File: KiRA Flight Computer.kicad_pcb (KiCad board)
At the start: 4 copper layers, 50 x 74.8 mm, 112 parts, among them IC1 SC4216HSETRT, J1 Conn_01x04_Pin, J10 Conn_01x02_Pin, J11 Conn_01x03_Pin, J12 Conn_01x03_Pin, J13 Screw_Terminal_01x02, J14 Screw_Terminal_01x02, J15 Conn_Coaxial, J2 USB_C_Receptacle_USB2.0_14P, J3 Conn_01x03_Pin, J4 Conn_01x03, J5 Conn_01x02, J6 Micro_SD_Card_Det1, J8 Conn_01x02_Pin, J9 Conn_01x03_Pin, Q1 FDMA430NZ, Q2 FDMA430NZ, SW1 SW_Push, SW2 SW_SPDT, U1 ICM-426788P, U10 BNO055, U2 STM32F407VGTx, U3 MMC5883MA, U4 DPS368, U5 NEO-M9N, U6 Wio-SX1262, U7 USBLC6-2P6, U8 TPS62933P, U9 Tudi AT24CM02-SSHD-T-TUDI, Y1 16MHz 7pF, Y2 OV_7604

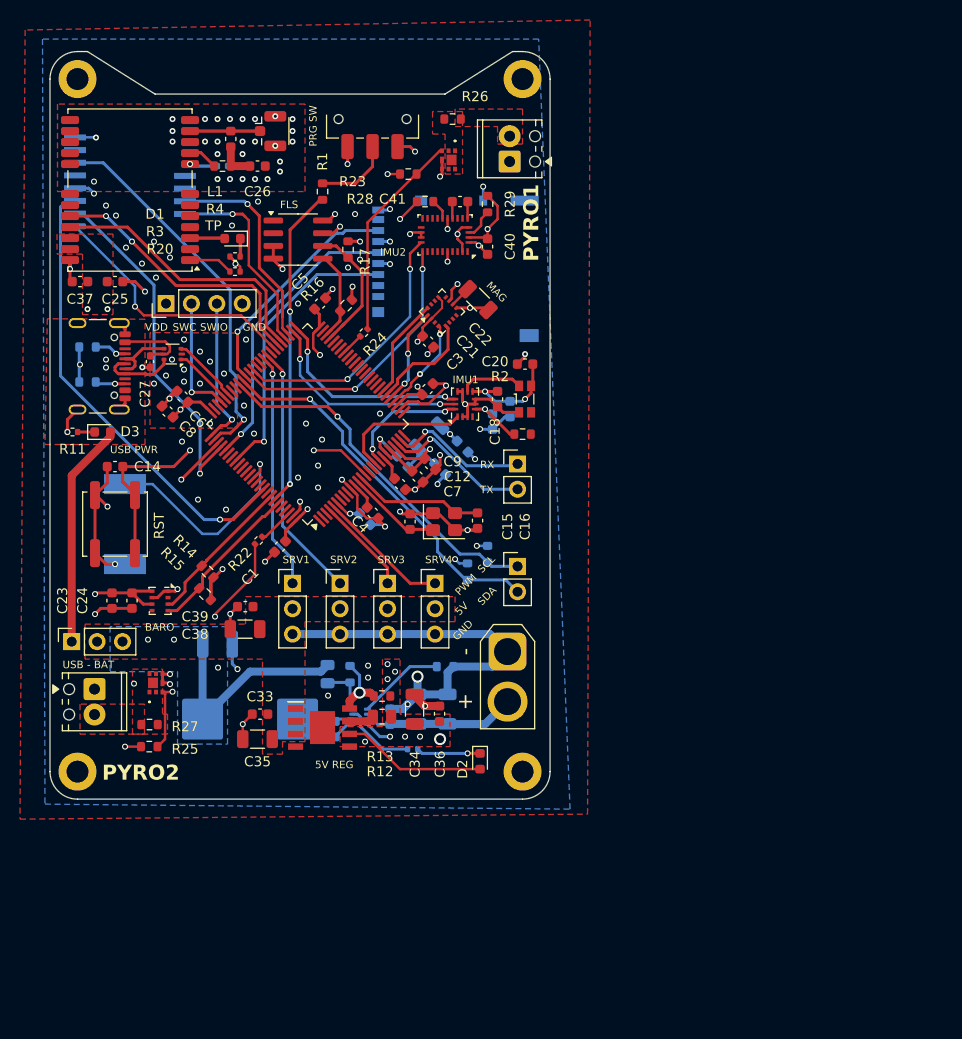
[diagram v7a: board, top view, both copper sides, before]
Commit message: Fix
- Add decoupling cap
- Component layout
- Redraw zones
- New buck converter
- Layout tweaks
- Change connector
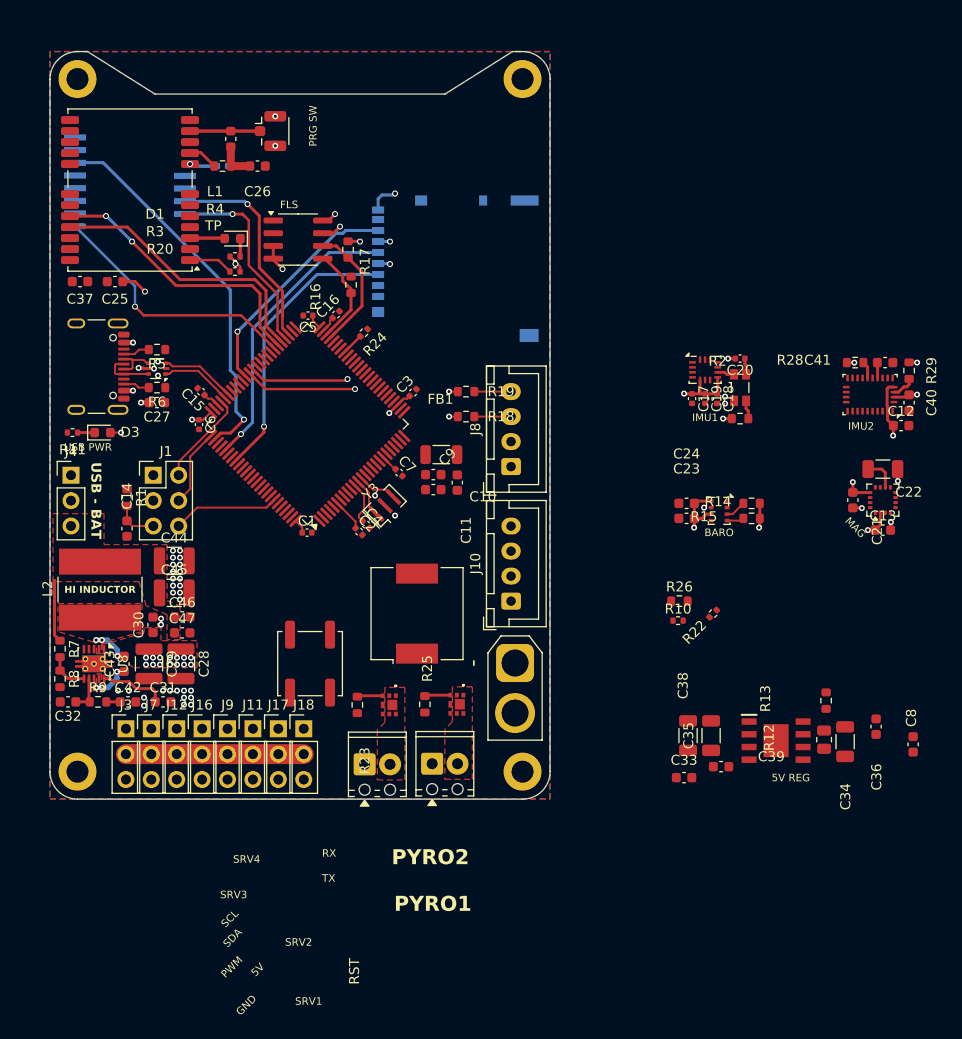
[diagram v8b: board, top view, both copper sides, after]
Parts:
- removed D2: LED_RED, LED_SMD:LED_0603_1608Metric
- removed R27: 1R, Resistor_SMD:R_0603_1608Metric
- removed SW2: SW_SPDT, Button_Switch_SMD:SW_SPDT_CK_JS102011SAQN
- removed Y1: 16MHz 7pF, Crystal:Crystal_SMD_3225-4Pin_3.2x2.5mm
- added C42: 12nF, Capacitor_SMD:C_0603_1608Metric, F.Cu at (68.8, 103.0)
- added C43: 100nF, Capacitor_SMD:C_0603_1608Metric, F.Cu at (68.4, 99.2)
- added C44: 47uF, Capacitor_SMD:C_1210_3225Metric, F.Cu at (73.4, 88.9)
- added C45: 47uF, Capacitor_SMD:C_1210_3225Metric, F.Cu at (73.4, 92.1)
- added C46: 100nF, Capacitor_SMD:C_0603_1608Metric, F.Cu at (74.2, 94.5)
- added C47: 100nF, Capacitor_SMD:C_0603_1608Metric, F.Cu at (74.2, 96.1)
- added J16: Conn_01x03, Connector_PinHeader_2.54mm:PinHeader_1x03_P2.54mm_Vertical, F.Cu at (76.2, 105.7)
- added J17: Conn_01x03, Connector_PinHeader_2.54mm:PinHeader_1x03_P2.54mm_Vertical, F.Cu at (83.8, 105.7)
- added J18: Conn_01x03, Connector_PinHeader_2.54mm:PinHeader_1x03_P2.54mm_Vertical, F.Cu at (86.4, 105.7)
- added J7: Conn_01x03, Connector_PinHeader_2.54mm:PinHeader_1x03_P2.54mm_Vertical, F.Cu at (71.1, 105.7)
- added Y3: Resonator, Crystal:Resonator_SMD_Murata_CSTxExxV-3Pin_3.0x1.1mm, F.Cu at (94.5, 83.4)
- BZ1, C10, C11, C30, FB1, R10, R18, R19, R5, R6: moved to F.Cu
- C1, C18, C20, C3, C4, C5, C6, C7: footprint Capacitor_SMD:C_0603_1608Metric -> Capacitor_SMD:C_0402_1005Metric
- C13: value 1uF -> 100nF; moved to F.Cu
- C15, C16: value 6pF -> 2.2uF; footprint Capacitor_SMD:C_0603_1608Metric -> Capacitor_SMD:C_0402_1005Metric
- C17, C19, C2: footprint Capacitor_SMD:C_0603_1608Metric -> Capacitor_SMD:C_0402_1005Metric; moved to F.Cu
- C27: footprint Capacitor_SMD:C_0402_1005Metric_Pad0.74x0.62mm_HandSolder -> Capacitor_SMD:C_0603_1608Metric
- C28, C29: footprint Capacitor_SMD:C_1206_3216Metric -> Capacitor_SMD:C_1210_3225Metric; moved to F.Cu
- C31: value 47uF -> 10nF; footprint Capacitor_SMD:C_1210_3225Metric -> Capacitor_SMD:C_0603_1608Metric; moved to F.Cu
- C32: value 100nF -> 120pF; moved to F.Cu
- J1: value Conn_01x04_Pin -> Conn_02x03_Odd_Even; footprint Connector_PinHeader_2.54mm:PinHeader_1x04_P2.54mm_Vertical -> Connector_PinHeader_2.54mm:PinHeader_2x03_P2.54mm_Vertical
- J10, J8: value Conn_01x02_Pin -> Conn_01x04; footprint Connector_PinHeader_2.54mm:PinHeader_1x02_P2.54mm_Vertical -> Connector_JST:JST_XH_B4B-XH-A_1x04_P2.50mm_Vertical
- J11, J12, J3, J9: value Conn_01x03_Pin -> Conn_01x03
- J4: footprint Connector_PinSocket_2.54mm:PinSocket_1x03_P2.54mm_Vertical -> Connector_PinHeader_2.54mm:PinHeader_1x03_P2.54mm_Vertical
- L2: value 7.8uH -> 15uH; footprint Inductor_SMD:L_APV_APH1050 -> Inductor_SMD:L_Bourns-SRN8040_8x8.15mm; moved to F.Cu
- R1: value 10k -> 4.7k
- R26: value 1R -> 4.7k
- R7: value 0R -> 100K; moved to F.Cu
- R8: value 52k -> 19.1K; footprint Resistor_SMD:R_0805_2012Metric -> Resistor_SMD:R_0603_1608Metric; moved to F.Cu
- R9: value 10k -> 3.47K; moved to F.Cu
- U8: value TPS62933P -> TPS54336ADRCR; footprint Package_TO_SOT_SMD:SOT-583-8 -> Package_SON:VSON-10-1EP_3x3mm_P0.5mm_EP1.65x2.4mm_ThermalVias; moved to F.Cu
- moved C8 81.6 mm to (147.3, 107.3), turned to -90 degrees
- moved J13 62.0 mm to (92.5, 109.3), turned to 0 degrees
- moved C23 58.0 mm to (124.7, 84.7), turned to 180 degrees
- moved U4 56.6 mm to (127.9, 83.9)
- moved C24 56.3 mm to (124.7, 83.2), turned to 180 degrees
- moved R15 55.2 mm to (131.2, 84.7), turned to 180 degrees
- moved R14 54.8 mm to (131.2, 83.2), turned to 180 degrees
- moved Q1 54.8 mm to (94.9, 103.3)
- moved R23 53.3 mm to (91.7, 103.3), turned to -90 degrees
- moved R26 53.3 mm to (123.9, 93.0), turned to 0 degrees
- moved C39 50.2 mm to (128.1, 109.5), turned to 0 degrees
- moved C12 48.6 mm to (146.1, 75.4), turned to 0 degrees
- moved C13 48.5 mm to (144.3, 85.8), turned to 0 degrees
- moved U3 47.9 mm to (144.3, 82.8), turned to 90 degrees
- moved R22 46.0 mm to (127.3, 94.2)
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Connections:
- net /SWCLK renamed SWCLK
- BZ1 pad 1: BUZZER -> +5V
- BZ1 pad 2: GND -> /Pinout/PYOUT2
- C10 pad 1: VREF+ -> +3.3VA
- C12 pad 1: VREF+ -> +3.3V
- C13 pad 1: VREF+ -> +3.3V
- C14 pad 1: /NRST -> NRST
- C15 pad 1: RCC IN -> Net-(U2-VCAP_2)
- C16 pad 1: RCC OUT -> Net-(U2-VCAP_1)
- C31 pad 1: +V_REG -> Net-(U8-SS)
- C32 pad 1: Net-(U8-BST) -> Net-(U8-COMP)
- C32 pad 2: Net-(U8-SW) -> GND
- C7 pad 1: unconnected-(C7-Pad1) -> +3.3V
- C9 pad 1: VREF+ -> +3.3VA
- FB1 pad 1: VREF+ -> +3.3VA
- J1 pad 1: +3.3V -> GND
- J1 pad 3: /SWIO -> +3.3V
- J1 pad 4: GND -> SWDIO
- J10 pad 1: UART4_RX -> GND
- J10 pad 2: UART4_TX -> +3.3V
- J11 pad 1: PWM3 -> PWM6
- J12 pad 1: PWM4 -> PWM3
- J13 pad 2: Net-(J13-Pin_2) -> /Pinout/PYOUT1
- J14 pad 2: Net-(J14-Pin_2) -> /Pinout/PYOUT2
- J8 pad 1: I2C3_SCL -> GND
- J8 pad 2: I2C3_SDA -> +3.3V
- J9 pad 1: PWM2 -> PWM5
- L2 pad 1: Net-(U8-SW) -> Net-(U8-PH)
- R1 pad 1: Net-(SW2-B) -> +3.3V
- R1 pad 2: /BOOT0 -> NRST
- R10 pad 1: Net-(U8-PG) -> BUZZER
- R10 pad 2: Net-(D2-K) -> Net-(Q3-G)
- R26 pad 1: Net-(J13-Pin_2) -> Net-(Q3-G)
- R26 pad 2: /Pinout/PYOUT1 -> GND
- R7 pad 1: Net-(U8-RT) -> +V_REG
- R7 pad 2: GND -> Net-(U8-VSENSE)
- R8 pad 1: +V_REG -> Net-(U8-VSENSE)
- R8 pad 2: Net-(U8-FB) -> GND
- R9 pad 1: Net-(U8-FB) -> Net-(U8-COMP)
- R9 pad 2: GND -> Net-(C42-Pad1)
- SW1 pad 2: /NRST -> NRST
- U2 pad 14: /NRST -> NRST
- U2 pad 21: VREF+ -> +3.3VA
- U2 pad 22: VREF+ -> +3.3VA
- U2 pad 49: unconnected-(U2-VCAP_1-Pad49) -> Net-(U2-VCAP_1)
- U2 pad 73: unconnected-(U2-VCAP_2-Pad73) -> Net-(U2-VCAP_2)
- U2 pad 76: /SWIO -> SWDIO
- U2 pad 94: /BOOT0 -> BOOT
- U8 pad 1: Net-(U8-RT) -> +BAT
- U8 pad 2: unconnected-(U8-EN-Pad2) -> Net-(U8-PH)
- U8 pad 3: +BAT -> GND
- U8 pad 5: Net-(U8-SW) -> GND
- U8 pad 6: Net-(U8-BST) -> Net-(U8-VSENSE)
- U8 pad 7: Net-(U8-PG) -> Net-(U8-COMP)
- U8 pad 8: Net-(U8-FB) -> unconnected-(U8-EN-Pad8)
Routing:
- net GND: track 189.9 -> 18.2 mm, vias 124 -> 49
- net +BAT: track 121.5 -> 0.00 mm, vias 0 -> 14
- net +3.3V: track 109.3 -> 55.5 mm, vias 33 -> 17
- net SPI3_MOSI: track 46.1 -> 0.00 mm, vias 1 -> 0
- net SPI3_SCK: track 40.6 -> 0.00 mm, vias 2 -> 0
- net SPI3_MISO: track 35.2 -> 0.00 mm, vias 1 -> 0
- net /NRST: track 35.1 -> 0.00 mm, vias 2 -> 0
- net I2C3_SDA: track 37.7 -> 3.67 mm, vias 1 -> 0
- net I2C3_SCL: track 36.3 -> 3.67 mm, vias 1 -> 0
- net /BOOT0: track 32.1 -> 0.00 mm, vias 2 -> 0
- net PWM2: track 25.8 -> 0.00 mm, vias 1 -> 0
- net VBUS: track 29.9 -> 5.30 mm, vias 0 -> 6
- net PWM1: track 23.6 -> 0.00 mm, vias 1 -> 0
- net Net-(Q2-G): track 25.0 -> 2.64 mm, vias 2 -> 0
- net BUZZER: track 21.8 -> 0.00 mm, vias 1 -> 0
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- added copper zone on In2.Cu, net +5V
- added copper zone on F.Cu, net +BAT
- added copper zone on In2.Cu, net +BAT
- added copper zone on F.Cu, net +V_REG
- added copper zone on F.Cu, net Net-(U8-BOOT)
- added copper zone on F.Cu, net Net-(U8-PH)
- added copper zone on In2.Cu, net VBUS
- removed copper zone on F.Cu, net +3.3V
- removed copper zone on F.Cu, net +5V
- removed copper zone on B.Cu, net +V_REG
- removed copper zone on F.Cu, net /Pinout/PYOUT2
- removed copper zone on F.Cu, net Net-(J13-Pin_2)
- removed copper zone on F.Cu, net Net-(J14-Pin_2)
- removed copper zone on F.Cu, net VBUS
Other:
- board text added: "HI INDUCTOR"
- board text removed: "+"
- board text removed: "SWC"
- board text removed: "SWIO"
- board text removed: "VDD"
